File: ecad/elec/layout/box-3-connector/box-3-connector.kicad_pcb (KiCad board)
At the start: 2 copper layers, 72.5 x 7.9 mm, 2 parts

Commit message: improve workflow
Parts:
- moved CN1 0.50 mm to (0.66, 0.71), turned to 180 degrees
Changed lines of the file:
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@@
 	(footprint "TE_Connectivity_5_1734857_1:CONN-SMD_5-1734857-1"
 		(layer "F.Cu")
-		(at 0.2921 1.05007)
+		(at 0.6585 0.7056 180)
 		(property "Reference" "CN1"
-			(at -12.6 -5 0)
+			(at -12.6 -5 180)
 			(layer "F.SilkS")
 			(effects
@@
 		)
 		(property "Value" ""
-			(at 0 4 0)
+			(at 0 4 180)
 			(layer "F.Fab")
 			(effects
@@
 		)
 		(property "Datasheet" ""
-			(at 0 0 0)
+			(at 0 0 180)
 			(layer "F.Fab")
 			(hide yes)
@@
 		)
 		(property "Description" ""
-			(at 0 0 0)
+			(at 0 0 180)
 			(layer "F.Fab")
 			(hide yes)
@@
 		)
 		(property "LCSC" "C4645333"
-			(at 0 0 0)
+			(at 0 0 180)
 			(layer "User.9")
 			(hide yes)
@@
 		)
 		(property "Manufacturer" "TE Connectivity"
-			(at 0 0 0)
+			(at 0 0 180)
 			(layer "User.9")
 			(hide yes)
@@
 		)
 		(property "Partnumber" "5-1734857-1"
-			(at 0 0 0)
+			(at 0 0 180)
 			(layer "User.9")
 			(hide yes)
@@
 		)
 		(property "atopile_address" "conn"
-			(at 0 0 0)
+			(at 0 0 180)
 			(layer "User.9")
 			(hide yes)
@@
 		)
 		(property "lcsc_id" "C4645333"
-			(at 0 0 0)
+			(at 0 0 180)
 			(layer "User.9")
 			(hide yes)
@@
 		)
 		(pad "A1" smd rect
-			(at -9.5 0 0)
+			(at -9.5 0 180)
 			(size 0.7 3)
 			(layers "F.Cu" "F.Paste" "F.Mask")
@@
 		)
 		(pad "A2" smd rect
-			(at -8.5 0 0)
+			(at -8.5 0 180)
 			(size 0.7 3)
 			(layers "F.Cu" "F.Paste" "F.Mask")
@@
 		)
 		(pad "A3" smd rect
-			(at -7.5 0 0)
+			(at -7.5 0 180)
 			(size 0.7 3)
 			(layers "F.Cu" "F.Paste" "F.Mask")
@@
 		)
 		(pad "A4" smd rect
-			(at -6.5 0 0)
+			(at -6.5 0 180)
 			(size 0.7 3)
 			(layers "F.Cu" "F.Paste" "F.Mask")
@@
 		)
 		(pad "A5" smd rect
-			(at -5.5 0 0)
+			(at -5.5 0 180)
 			(size 0.7 3)
 			(layers "F.Cu" "F.Paste" "F.Mask")
@@
 		)
 		(pad "A6" smd rect
-			(at -4.5 0 0)
+			(at -4.5 0 180)
 			(size 0.7 3)
 			(layers "F.Cu" "F.Paste" "F.Mask")
@@
 		)
 		(pad "A7" smd rect
-			(at -3.5 0 0)
+			(at -3.5 0 180)
 			(size 0.7 3)
 			(layers "F.Cu" "F.Paste" "F.Mask")
@@
 		)
 		(pad "A8" smd rect
-			(at -2.5 0 0)
+			(at -2.5 0 180)
 			(size 0.7 3)
 			(layers "F.Cu" "F.Paste" "F.Mask")
@@
 		)
 		(pad "A9" smd rect
-			(at -1.5 0 0)
+			(at -1.5 0 180)
 			(size 0.7 3)
 			(layers "F.Cu" "F.Paste" "F.Mask")
@@
 		)
 		(pad "A10" smd rect
-			(at -0.5 0 0)
+			(at -0.5 0 180)
 			(size 0.7 3)
 			(layers "F.Cu" "F.Paste" "F.Mask")
@@
 		)
 		(pad "A11" smd rect
-			(at 0.5 0 0)
+			(at 0.5 0 180)
 			(size 0.7 3)
 			(layers "F.Cu" "F.Paste" "F.Mask")
@@
 		)
 		(pad "A12" smd rect
-			(at 3.5 0 0)
+			(at 3.5 0 180)
 			(size 0.7 3)
 			(layers "F.Cu" "F.Paste" "F.Mask")
@@
 		)
 		(pad "A13" smd rect
-			(at 4.5 0 0)
+			(at 4.5 0 180)
 			(size 0.7 3)
 			(layers "F.Cu" "F.Paste" "F.Mask")
@@
 		)
 		(pad "A14" smd rect
-			(at 5.5 0 0)
+			(at 5.5 0 180)
 			(size 0.7 3)
 			(layers "F.Cu" "F.Paste" "F.Mask")
@@
 		)
 		(pad "A15" smd rect
-			(at 6.5 0 0)
+			(at 6.5 0 180)
 			(size 0.7 3)
 			(layers "F.Cu" "F.Paste" "F.Mask")
@@
 		)
 		(pad "A16" smd rect
-			(at 7.5 0 0)
+			(at 7.5 0 180)
 			(size 0.7 3)
 			(layers "F.Cu" "F.Paste" "F.Mask")
@@
 		)
 		(pad "A17" smd rect
-			(at 8.5 0 0)
+			(at 8.5 0 180)
 			(size 0.7 3)
 			(layers "F.Cu" "F.Paste" "F.Mask")
@@
 		)
 		(pad "A18" smd rect
-			(at 9.5 0 0)
+			(at 9.5 0 180)
 			(size 0.7 3)
 			(layers "F.Cu" "F.Paste" "F.Mask")
@@
 		)
 		(pad "B1" smd rect
-			(at -9.5 0 0)
+			(at -9.5 0 180)
 			(size 0.7 3)
 			(layers "B.Cu" "B.Paste" "B.Mask")
@@
 		)
 		(pad "B2" smd rect
-			(at -8.5 0 0)
+			(at -8.5 0 180)
 			(size 0.7 3)
 			(layers "B.Cu" "B.Paste" "B.Mask")
@@
 		)
 		(pad "B3" smd rect
-			(at -7.5 0 0)
+			(at -7.5 0 180)
 			(size 0.7 3)
 			(layers "B.Cu" "B.Paste" "B.Mask")
@@
 		)
 		(pad "B4" smd rect
-			(at -6.5 0 0)
+			(at -6.5 0 180)
 			(size 0.7 3)
 			(layers "B.Cu" "B.Paste" "B.Mask")
@@
 		)
 		(pad "B5" smd rect
-			(at -5.5 0 0)
+			(at -5.5 0 180)
 			(size 0.7 3)
 			(layers "B.Cu" "B.Paste" "B.Mask")
@@
 		)
 		(pad "B6" smd rect
-			(at -4.5 0 0)
+			(at -4.5 0 180)
 			(size 0.7 3)
 			(layers "B.Cu" "B.Paste" "B.Mask")
@@
 		)
 		(pad "B7" smd rect
-			(at -3.5 0 0)
+			(at -3.5 0 180)
 			(size 0.7 3)
 			(layers "B.Cu" "B.Paste" "B.Mask")
@@
 		)
 		(pad "B8" smd rect
-			(at -2.5 0 0)
+			(at -2.5 0 180)
 			(size 0.7 3)
 			(layers "B.Cu" "B.Paste" "B.Mask")
@@
 		)
 		(pad "B9" smd rect
-			(at -1.5 0 0)
+			(at -1.5 0 180)
 			(size 0.7 3)
 			(layers "B.Cu" "B.Paste" "B.Mask")
@@
 		)
 		(pad "B10" smd rect
-			(at -0.5 0 0)
+			(at -0.5 0 180)
 			(size 0.7 3)
 			(layers "B.Cu" "B.Paste" "B.Mask")
@@
 		)
 		(pad "B11" smd rect
-			(at 0.5 0 0)
+			(at 0.5 0 180)
 			(size 0.7 3)
 			(layers "B.Cu" "B.Paste" "B.Mask")
@@
 		)
 		(pad "B12" smd rect
-			(at 3.5 0 0)
+			(at 3.5 0 180)
 			(size 0.7 3)
 			(layers "B.Cu" "B.Paste" "B.Mask")
@@
 		)
 		(pad "B13" smd rect
-			(at 4.5 0 0)
+			(at 4.5 0 180)
 			(size 0.7 3)
 			(layers "B.Cu" "B.Paste" "B.Mask")
@@
 		)
 		(pad "B14" smd rect
-			(at 5.5 0 0)
+			(at 5.5 0 180)
 			(size 0.7 3)
 			(layers "B.Cu" "B.Paste" "B.Mask")
@@
 		)
 		(pad "B15" smd rect
-			(at 6.5 0 0)
+			(at 6.5 0 180)
 			(size 0.7 3)
 			(layers "B.Cu" "B.Paste" "B.Mask")
@@
 		)
 		(pad "B16" smd rect
-			(at 7.5 0 0)
+			(at 7.5 0 180)
 			(size 0.7 3)
 			(layers "B.Cu" "B.Paste" "B.Mask")
@@
 		)
 		(pad "B17" smd rect
-			(at 8.5 0 0)
+			(at 8.5 0 180)
 			(size 0.7 3)
 			(layers "B.Cu" "B.Paste" "B.Mask")
@@
 		)
 		(pad "B18" smd rect
-			(at 9.5 0 0)
-			(size 0.7 3)
-			(layers "B.Cu" "B.Paste" "B.Mask")
+			(at 9.5 0 180)
+			(size 0.7 3)
+			(layers "B.Cu" "B.Paste" "B.Mask")

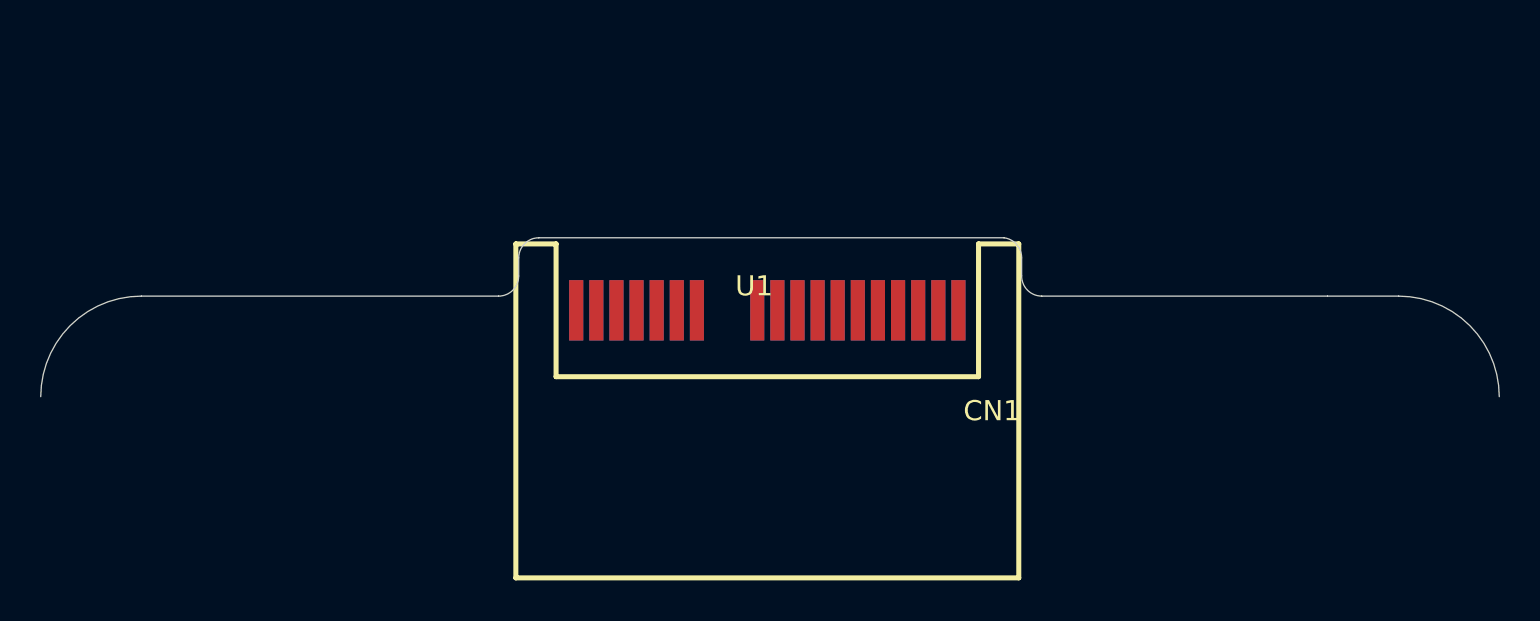
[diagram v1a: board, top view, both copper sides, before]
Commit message: improve placement of components and robustness of scripts
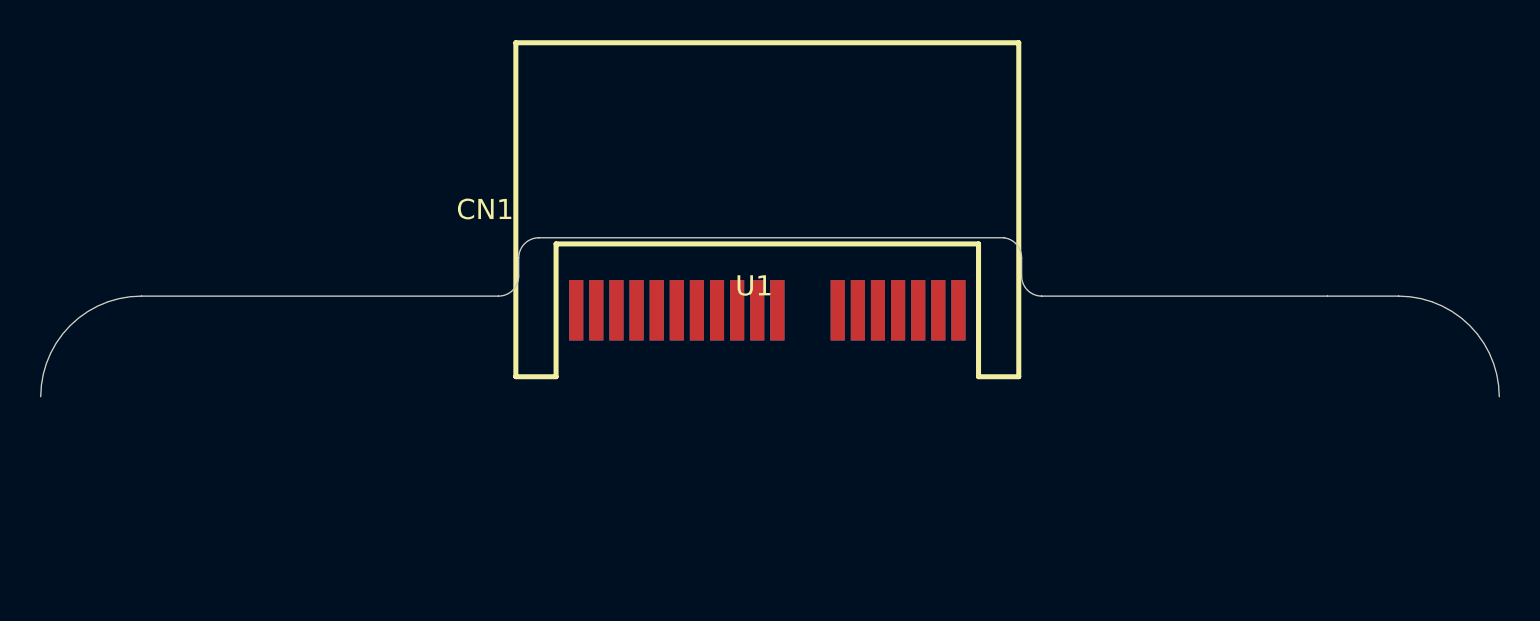
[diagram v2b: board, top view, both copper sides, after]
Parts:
- turned CN1 to 0 degrees
